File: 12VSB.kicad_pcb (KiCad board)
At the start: 2 copper layers, 24 parts, among them U1 FP6296

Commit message: updated pcb layout
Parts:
- H1, H2, H3, H4: footprint MountingHole:MountingHole_3.5mm_Pad -> MountingHole:MountingHole_2.2mm_M2_DIN965_Pad
- L1: moved to B.Cu
- moved U1 54.4 mm to (69.9, 65.4)
- moved L1 43.3 mm to (67.1, 63.5)
- moved H4 31.3 mm to (80.0, 50.8)
- moved C2 25.4 mm to (57.1, 63.5), turned to 90 degrees
- moved D1 24.2 mm to (63.6, 73.4)
- moved D2 24.2 mm to (62.7, 81.8)
- moved H3 24.2 mm to (54.6, 59.7)
- moved C3 22.1 mm to (62.8, 65.5)
- moved C1 22.1 mm to (59.7, 63.5), turned to 90 degrees
- moved H1 20.8 mm to (54.6, 50.8)
- moved H2 20.4 mm to (54.6, 67.3)
- moved R10 18.3 mm to (62.8, 67.1)
- moved C4 18.3 mm to (76.1, 67.8)
- moved C6 14.6 mm to (78.7, 62.9), turned to -90 degrees
- moved R8 13.8 mm to (67.6, 59.9), turned to 180 degrees
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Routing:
- net 5VSB: track 0.00 -> 16.8 mm
- net Net-(D1-A): vias 0 -> 1

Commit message: updated pcb layout
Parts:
- C1, C2, C5, C6, D2: moved to B.Cu
- moved D2 29.0 mm to (61.2, 52.8)
- moved R2 24.7 mm to (63.6, 66.3), turned to 180 degrees
- moved R4 24.5 mm to (65.8, 67.8)
- moved R3 23.9 mm to (67.6, 64.8)
- moved C10 22.2 mm to (63.6, 67.6), turned to 180 degrees
- moved R1 21.8 mm to (65.8, 66.3), turned to 180 degrees
- moved D1 20.7 mm to (61.2, 52.8), turned to 180 degrees
- moved C5 15.6 mm to (66.5, 56.6)
- moved C6 12.0 mm to (68.5, 56.6)
- moved H4 12.0 mm to (68.1, 52.1)
- moved U1 8.52 mm to (62.0, 62.2)
- moved C4 8.29 mm to (67.8, 67.0), turned to 90 degrees
- moved C9 8.21 mm to (68.1, 62.0)
- moved R5 8.12 mm to (68.1, 60.2)
- moved C12 8.02 mm to (63.2, 57.7)
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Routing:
- net GNDREF: track 0.00 -> 11.7 mm
- net Net-(D1-A): track 0.00 -> 10.9 mm, vias 1 -> 0
- net Net-(U1-COMP): track 0.00 -> 8.77 mm
- net Net-(U1-OC): track 0.00 -> 5.11 mm
- net Net-(U1-VCC): track 0.00 -> 5.00 mm
- net 5VSB: track 16.8 -> 21.6 mm
- net Net-(U1-HVDD): track 0.00 -> 4.50 mm
- net Net-(U1-EN): track 0.00 -> 3.93 mm
- net Net-(U1-FB): track 0.00 -> 3.41 mm
- net Net-(C12-Pad1): track 0.00 -> 1.71 mm
- net Net-(C4-Pad1): track 0.00 -> 1.65 mm

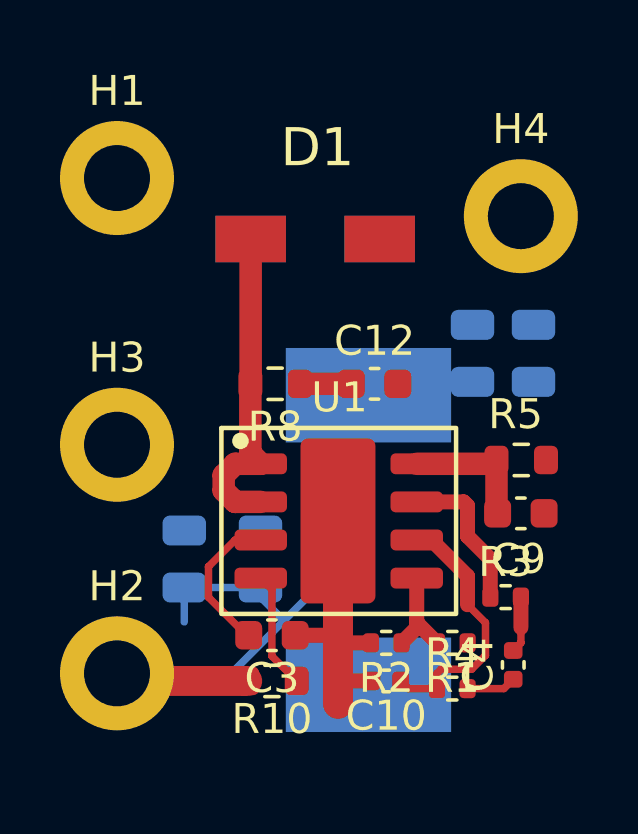
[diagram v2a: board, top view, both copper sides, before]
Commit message: Corrected Schema and updated PCB Layout
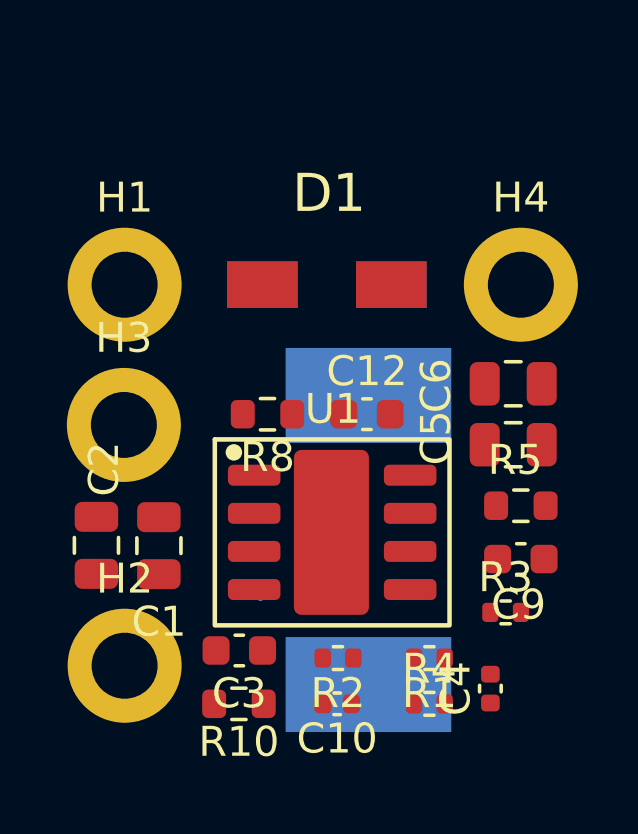
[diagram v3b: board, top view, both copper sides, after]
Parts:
- added L1: L 3R3, 12VSB Library:INDM125125X800N, B.Cu at (63.0, 62.9)
- C1, C2, C5, C6: moved to F.Cu
- moved C2 5.49 mm to (53.9, 63.0)
- moved H1 3.57 mm to (54.9, 54.4)
- moved C5 3.34 mm to (67.8, 59.7), turned to 0 degrees
- moved H4 2.29 mm to (68.1, 54.4)
- moved C10 1.81 mm to (61.9, 68.3)
- moved R2 1.69 mm to (62.0, 66.8)
- moved D1 1.57 mm to (61.6, 54.4)
- moved D2 1.57 mm to (61.6, 54.4)
- moved R5 1.52 mm to (68.1, 61.7)
- moved C9 1.52 mm to (68.1, 63.5)
- moved R10 1.34 mm to (58.7, 68.3)
- moved C6 1.22 mm to (67.8, 57.7), turned to 0 degrees
- moved C3 1.20 mm to (58.7, 66.5)
- moved C4 1.10 mm to (67.1, 67.8)
- moved C12 1.05 mm to (62.9, 58.7)
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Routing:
- net 5VSB: track 21.6 -> 0.68 mm
- net GNDREF: track 11.7 -> 0.00 mm
- net Net-(D1-A): track 10.9 -> 0.00 mm
- net Net-(U1-COMP): track 8.77 -> 0.00 mm
- net Net-(U1-OC): track 5.11 -> 0.00 mm
- net Net-(U1-VCC): track 5.00 -> 0.00 mm
- net Net-(U1-HVDD): track 4.50 -> 0.00 mm
- net Net-(U1-EN): track 3.93 -> 0.00 mm
- net Net-(U1-FB): track 3.41 -> 0.00 mm
- net Net-(C12-Pad1): track 1.71 -> 0.00 mm
- net Net-(C4-Pad1): track 1.65 -> 0.00 mm
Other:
- copper layers 2 -> 4

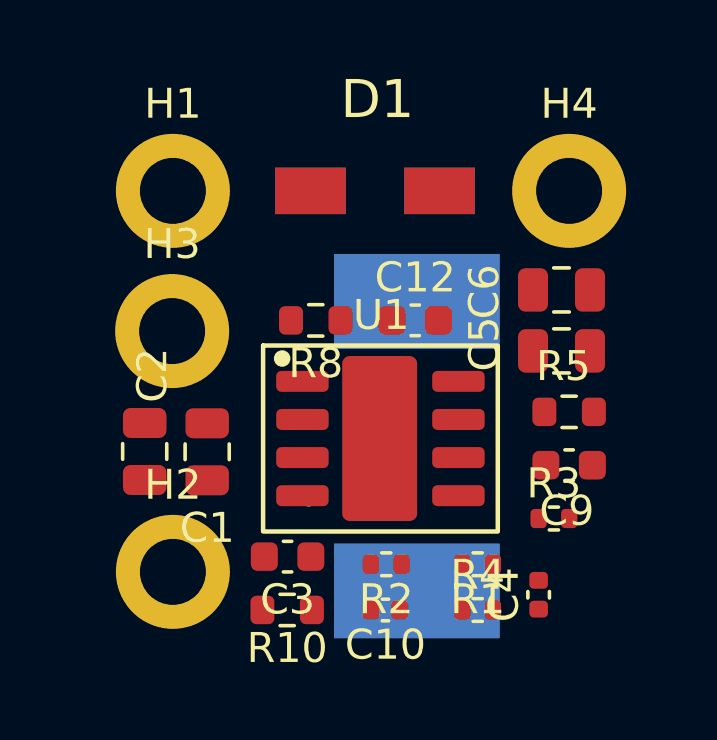
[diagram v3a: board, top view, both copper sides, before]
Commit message: initial pcb trace layout
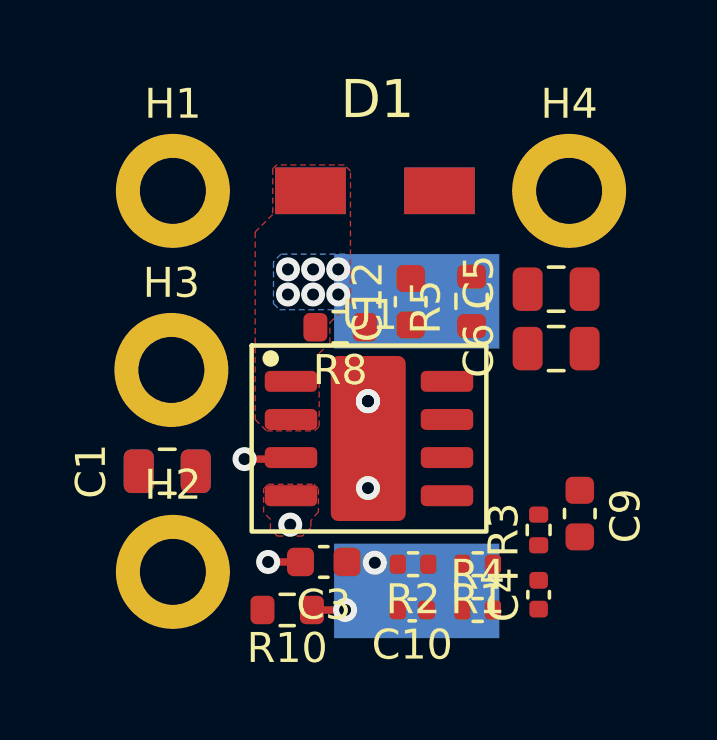
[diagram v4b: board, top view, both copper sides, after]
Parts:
- removed the L1 at (63.0, 62.9)
- C2: moved to B.Cu
- moved R5 4.91 mm to (64.8, 58.0), turned to -90 degrees
- moved C5 2.07 mm to (67.6, 57.6)
- moved C6 1.96 mm to (67.6, 59.6)
- moved C9 1.65 mm to (68.4, 65.1), turned to 90 degrees
- moved C1 1.48 mm to (54.7, 63.7), turned to 0 degrees
- moved H3 1.30 mm to (54.8, 60.3)
- moved C3 1.22 mm to (59.9, 66.7)
- moved C2 1.00 mm to (54.7, 63.7), turned to 0 degrees
- moved C10 0.89 mm to (62.8, 68.3)
- moved R2 0.89 mm to (62.9, 66.8)
- moved R8 0.84 mm to (60.4, 58.9)
- moved C12 0.64 mm to (62.8, 58.1), turned to 90 degrees
- moved R3 0.63 mm to (67.1, 65.7), turned to 90 degrees
- moved U1 0.38 mm to (61.4, 62.6)
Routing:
- net Net-(U1-VCC): track 0.00 -> 6.40 mm, vias 0 -> 2
- net Net-(U1-EN): track 0.00 -> 5.25 mm, vias 0 -> 2
- net 5VSB: track 0.68 -> 0.36 mm, vias 0 -> 1
- net Net-(D1-A): vias 0 -> 6
- net GNDREF: vias 0 -> 3
- added copper zone on B.Cu, net Net-(D1-A)
- added copper zone on F.Cu, net Net-(D1-A)
- added copper zone on F.Cu, net Net-(U1-EN)

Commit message: updated pcb track layout
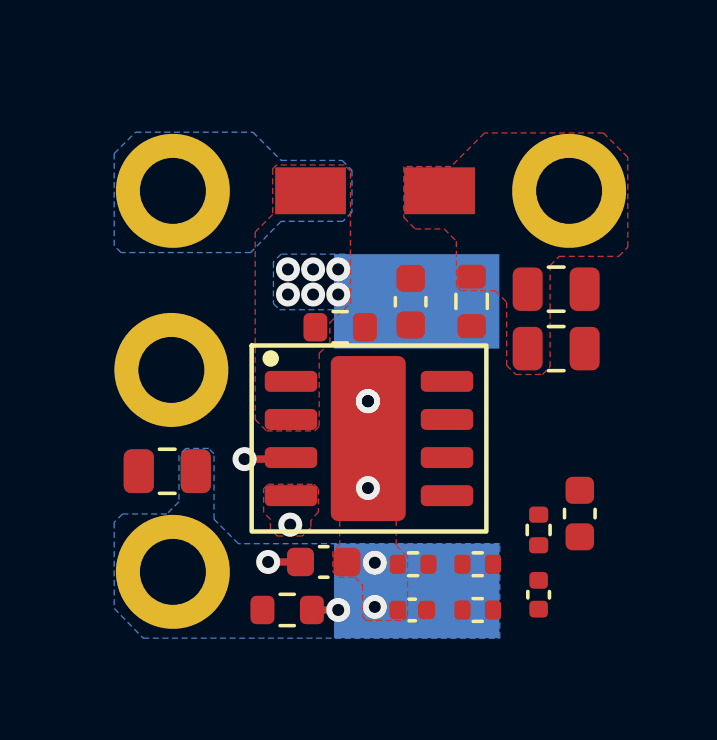
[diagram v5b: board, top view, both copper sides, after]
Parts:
- turned C1 to 180 degrees
- turned C2 to 180 degrees
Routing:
- net GNDREF: vias 3 -> 5
- net 5VSB: vias 1 -> 0
- added copper zone on B.Cu, net 12V
- added copper zone on F.Cu, net 12VSB
- added copper zone on B.Cu, net 5VSB
- added copper zone on F.Cu, net GNDREF

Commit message: Updated PCB Layout and Documentation
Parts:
- C2: moved to F.Cu
- moved C9 8.83 mm to (63.1, 58.1)
- moved R3 3.71 mm to (66.6, 62.0), turned to 0 degrees
- moved C5 1.76 mm to (68.7, 59.1), turned to -90 degrees
- moved C12 1.30 mm to (61.5, 58.1)
- moved C2 1.20 mm to (55.9, 63.5), turned to 90 degrees
- moved C6 1.15 mm to (66.6, 59.1), turned to -90 degrees
- moved R8 1.01 mm to (59.9, 58.1), turned to 90 degrees
- moved C1 0.88 mm to (53.8, 63.5), turned to 90 degrees
- moved H3 0.77 mm to (54.7, 59.6), turned to 90 degrees
- moved D1 0.67 mm to (60.9, 54.4)
- moved D2 0.67 mm to (60.9, 54.4)
- moved H4 0.66 mm to (67.5, 54.7)
- moved C4 0.61 mm to (67.7, 67.8)
- moved C3 0.39 mm to (59.5, 66.7)
- moved H1 0.32 mm to (54.8, 54.7)
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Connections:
- net GNDREF renamed GND
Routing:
- net 12VSB: track 0.00 -> 13.0 mm, vias 0 -> 1
- net Net-(U1-COMP): track 0.00 -> 9.58 mm
- net Net-(C4-Pad1): track 0.00 -> 2.13 mm
- net Net-(U1-OC): track 0.00 -> 2.09 mm
- net Net-(C12-Pad1): track 0.00 -> 1.62 mm
- net 5VSB: track 0.36 -> 1.72 mm
- net Net-(U1-EN): track 5.14 -> 4.26 mm, vias 2 -> 0
- net Net-(U1-VCC): track 6.40 -> 5.75 mm, vias 2 -> 0
- net GND: vias 5 -> 24
- added copper zone on B.Cu, net 12VSB
- added copper zone on F.Cu, net 5VSB
- added copper zone on In1.Cu, net GND
- added copper zone on In2.Cu, net GND
- added copper zone on F.Cu, net Net-(U1-FB)
- added copper zone on F.Cu, net Net-(U1-HVDD)
- removed copper zone on F.Cu, net Net-(U1-EN)
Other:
- board outline added: 16.9 x 16.9 mm
- board text added: "+12V"
- board text added: "+12VSB"
- board text added: "+5VSB"
- board text added: "GND"

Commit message: fixed diode footprint
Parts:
- moved H4 0.38 mm to (67.5, 54.3)
- moved H1 0.36 mm to (54.8, 54.3)
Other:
- board size 16.9 x 16.9 mm -> 16.9 x 17.3 mm

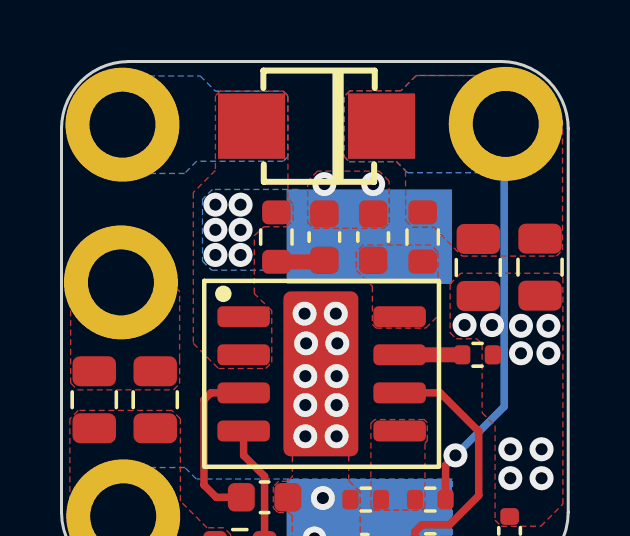
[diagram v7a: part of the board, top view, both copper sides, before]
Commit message: refined pcb tracks
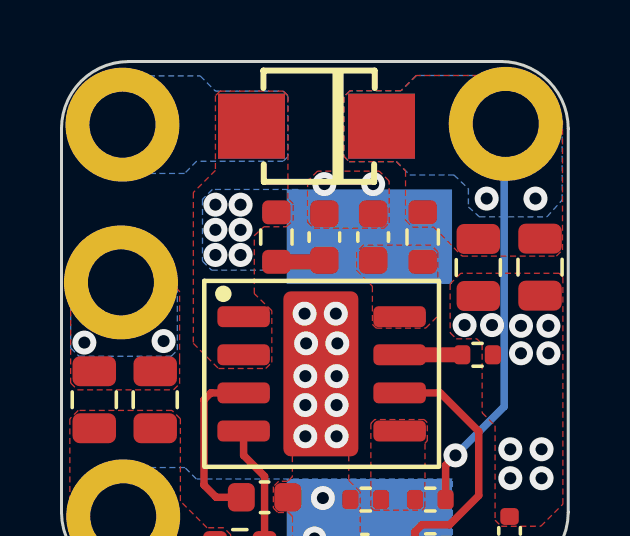
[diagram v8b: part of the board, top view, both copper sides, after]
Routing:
- net GND: vias 24 -> 26
- net 12VSB: vias 1 -> 3
- added copper zone on B.Cu, net GND
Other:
- board text added: "12VSB"
- board text removed: "+12VSB"
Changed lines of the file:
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@@
   (gr_line (start 69.6214 67.226444) (end 69.6214 54.437256)
     (stroke (width 0.1) (type default)) (layer "Edge.Cuts"))
-  (gr_text "+5VSB" (at 56.2356 65.278) (layer "B.SilkS")
-    (effects (font (size 0.6 0.6) (thickness 0.1) bold) (justify left bottom mirror))
-  )
-  (gr_text "+12VSB" (at 65.3542 52.451 90) (layer "B.SilkS")
-    (effects (font (size 0.6 0.6) (thickness 0.1)) (justify left bottom mirror))
-  )
-  (gr_text "GND" (at 55.6006 62.5094) (layer "B.SilkS")
-    (effects (font (size 0.6 0.6) (thickness 0.1) bold) (justify left bottom mirror))
-  )
-  (gr_text "+12V" (at 57.5818 52.8574 90) (layer "B.SilkS")
-    (effects (font (size 0.6 0.6) (thickness 0.1) bold) (justify left bottom mirror))
+  (gr_text "+5VSB" (at 56.769 65.2526) (layer "B.SilkS")
+    (effects (font (size 0.8 0.8) (thickness 0.1) bold) (justify left bottom mirror))
+  )
+  (gr_text "12VSB" (at 65.5828 52.5018 90) (layer "B.SilkS")
+    (effects (font (size 0.8 0.8) (thickness 0.1)) (justify left bottom mirror))
+  )
+  (gr_text "GND" (at 56.007 62.6872) (layer "B.SilkS")
+    (effects (font (size 0.8 0.8) (thickness 0.1) bold) (justify left bottom mirror))
+  )
+  (gr_text "+12V" (at 57.7342 52.7304 90) (layer "B.SilkS")
+    (effects (font (size 0.8 0.8) (thickness 0.1) bold) (justify left bottom mirror))
   )
   (segment (start 54.864 67.564) (end 54.61 67.31) (width 1) (layer "F.Cu") (net 1))
@@
   (via blind (at 61.4426 66.7512) (size 0.8) (drill 0.4) (layers "F.Cu" "In1.Cu") (free) (net 2))
   (via blind (at 61.4934 56.2864) (size 0.8) (drill 0.4) (layers "F.Cu" "In1.Cu") (net 2))
+  (via (at 56.134 61.5188) (size 0.8) (drill 0.4) (layers "F.Cu" "B.Cu") (free) (net 2))
   (via blind (at 63.119 56.2864) (size 0.8) (drill 0.4) (layers "F.Cu" "In2.Cu") (net 2))
   (via blind (at 68.0466 61.0108) (size 0.8) (drill 0.4) (layers "F.Cu" "In1.Cu") (net 2))
   (via blind (at 60.8584 62.6872) (size 0.8) (drill 0.4) (layers "F.Cu" "In2.Cu") (net 2))
+  (via (at 53.4924 61.5696) (size 0.8) (drill 0.4) (layers "F.Cu" "B.Cu") (free) (net 2))
   (via blind (at 61.8744 60.6044) (size 0.8) (drill 0.4) (layers "F.Cu" "In1.Cu") (net 2))
   (via blind (at 61.1632 68.0974) (size 0.8) (drill 0.4) (layers "F.Cu" "In1.Cu") (free) (net 2))
@@
   (segment (start 65.534 65.657) (end 65.534 66.802) (width 0.25) (layer "F.Cu") (net 5))
   (segment (start 65.8622 65.3288) (end 65.534 65.657) (width 0.25) (layer "F.Cu") (net 5))
+  (via (at 66.9036 56.769) (size 0.8) (drill 0.4) (layers "F.Cu" "B.Cu") (free) (net 5))
   (via (at 65.8622 65.3288) (size 0.8) (drill 0.4) (layers "F.Cu" "B.Cu") (free) (net 5))
+  (via (at 68.5292 56.769) (size 0.8) (drill 0.4) (layers "F.Cu" "B.Cu") (free) (net 5))
   (segment (start 67.4878 54.6608) (end 67.4878 63.7032) (width 0.25) (layer "B.Cu") (net 5))
   (segment (start 67.4878 63.7032) (end 65.8622 65.3288) (width 0.25) (layer "B.Cu") (net 5))
@@
     )
   )
+  (zone (net 2) (net_name "GND") (layer "B.Cu") (hatch edge 0.5)
+    (priority 14)
+    (connect_pads yes (clearance 0.5))
+    (min_thickness 0.25) (filled_areas_thickness no)
+    (fill yes (thermal_gap 0.5) (thermal_bridge_width 0.5))
+    (polygon
+      (pts
+        (xy 56.388 62.0268)
+        (xy 56.5912 61.8236)
+        (xy 56.5912 59.7408)
+        (xy 56.4134 59.563)
+        (xy 53.467 59.563)
+        (xy 53.0352 59.9948)
+        (xy 53.0352 61.7474)
+        (xy 53.3146 62.0268)
+      )
+    )
+  )
   (zone (net 5) (net_name "12VSB") (layer "B.Cu") (hatch edge 0.5)
     (priority 12)
@@
       (pts
         (xy 63.8937 55.5371)
-        (xy 64.262 55.9054)
-        (xy 67.7164 55.9054)
-        (xy 67.7164 53.594)
-        (xy 66.7893 52.6669)
+        (xy 64.3382 55.9816)
+        (xy 65.8114 55.9816)
+        (xy 66.294 56.4388)
+        (xy 66.294 57.0484)
+        (xy 66.661695 57.378432)
+        (xy 68.9102 57.378585)
+        (xy 69.4182 56.8198)
+        (xy 69.4182 54.356)
+        (xy 67.7291 52.6669)
         (xy 64.5541 52.6669)
         (xy 64.0461 53.1749)
